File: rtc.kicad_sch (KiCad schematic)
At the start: 8 parts, among them U2901 PCF85063ATL, Y2901 32.768kHz 7pF

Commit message: Fix schematic ERC errors
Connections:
- net I2C0.SCL renamed I2C1.SCL
- net I2C0.SDA renamed I2C1.SDA

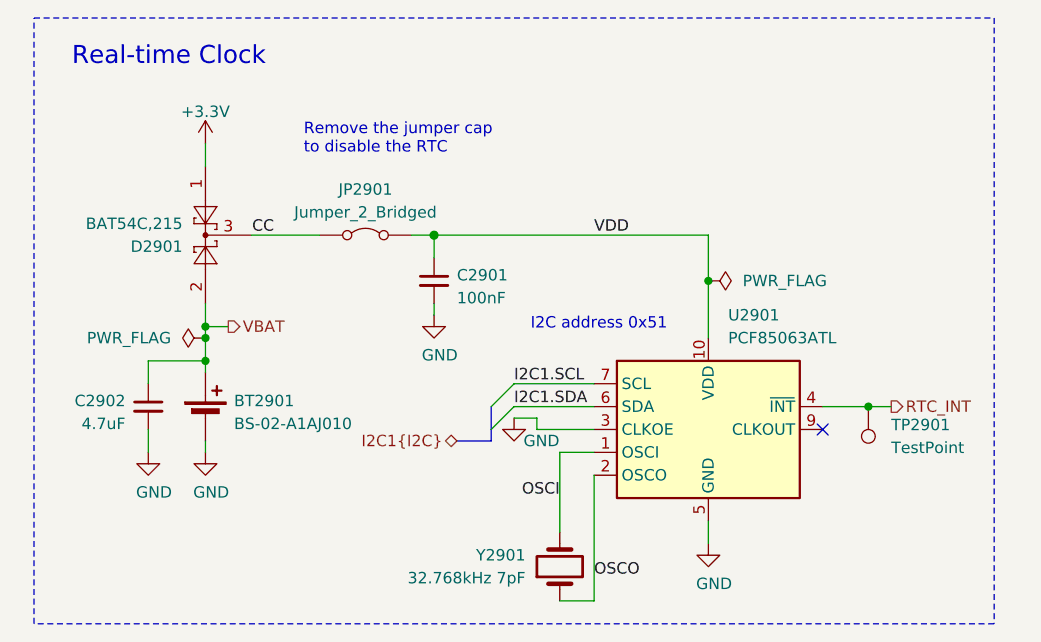
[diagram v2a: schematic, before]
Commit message: Reannotate components
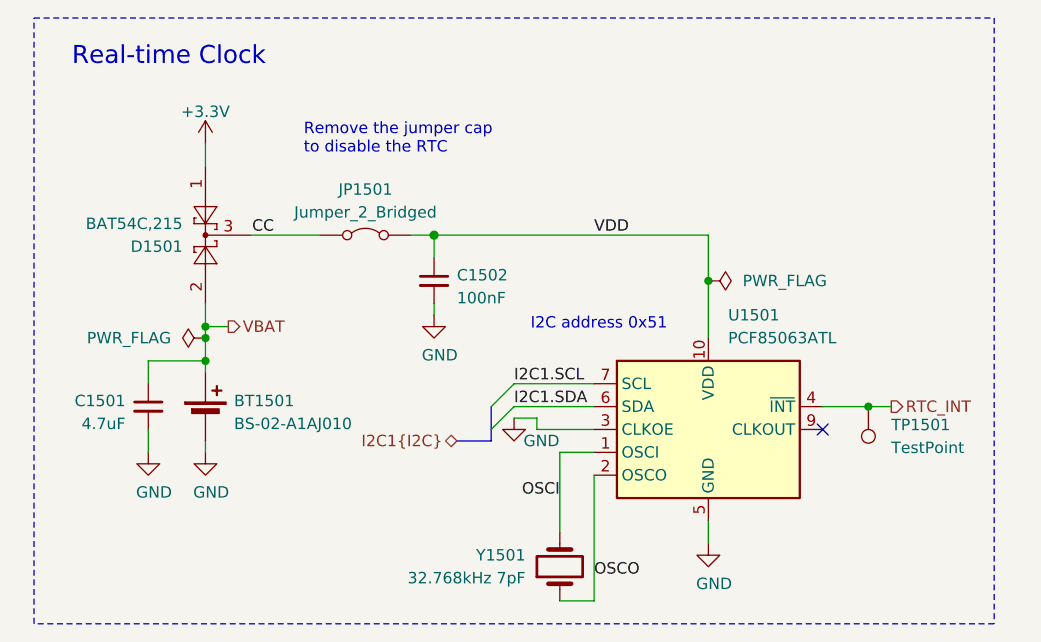
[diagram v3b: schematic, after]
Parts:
- renumbered BT2901 to BT1501, C2902 to C1501, C2901 to C1502, D2901 to D1501, JP2901 to JP1501, TP2901 to TP1501, U2901 to U1501, Y2901 to Y1501
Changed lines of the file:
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@@
 		(on_board yes)
 		(dnp no)
-		(property "Reference" "Y2901"
+		(property "Reference" "Y1501"
 			(at 147.32 118.1099 90)
 			(effects
@@
 			(project "HALPI2"
 				(path "/abc482bd-3f17-4d35-80db-1da3dcdb5c27/850df4bf-e40a-4082-adc2-76804638b949/e502b11a-b887-47b5-9ff1-f210171ce142"
-					(reference "Y2901")
+					(reference "Y1501")
 					(unit 1)
 				)
@@
 		(on_board yes)
 		(dnp no)
-		(property "Reference" "#FLG02901"
+		(property "Reference" "#FLG01502"
 			(at 169.545 87.63 0)
 			(effects
@@
 			(project "HALPI2"
 				(path "/abc482bd-3f17-4d35-80db-1da3dcdb5c27/850df4bf-e40a-4082-adc2-76804638b949/e502b11a-b887-47b5-9ff1-f210171ce142"
-					(reference "#FLG02901")
+					(reference "#FLG01502")
 					(unit 1)
 				)
@@
 		(on_board yes)
 		(dnp no)
-		(property "Reference" "D2901"
+		(property "Reference" "D1501"
 			(at 109.22 83.82 90)
 			(effects
@@
 			(project "HALPI2"
 				(path "/abc482bd-3f17-4d35-80db-1da3dcdb5c27/850df4bf-e40a-4082-adc2-76804638b949/e502b11a-b887-47b5-9ff1-f210171ce142"
-					(reference "D2901")
+					(reference "D1501")
 					(unit 1)
 				)
@@
 		(on_board yes)
 		(dnp no)
-		(property "Reference" "#PWR02907"
+		(property "Reference" "#PWR01506"
 			(at 167.64 123.19 0)
 			(effects
@@
 			(project "HALPI2"
 				(path "/abc482bd-3f17-4d35-80db-1da3dcdb5c27/850df4bf-e40a-4082-adc2-76804638b949/e502b11a-b887-47b5-9ff1-f210171ce142"
-					(reference "#PWR02907")
+					(reference "#PWR01506")
 					(unit 1)
 				)
@@
 		(on_board yes)
 		(dnp no)
-		(property "Reference" "TP2901"
+		(property "Reference" "TP1501"
 			(at 187.96 103.6319 0)
 			(effects
@@
 			(project "HALPI2"
 				(path "/abc482bd-3f17-4d35-80db-1da3dcdb5c27/850df4bf-e40a-4082-adc2-76804638b949/e502b11a-b887-47b5-9ff1-f210171ce142"
-					(reference "TP2901")
+					(reference "TP1501")
 					(unit 1)
 				)
@@
 		(on_board yes)
 		(dnp no)
-		(property "Reference" "BT2901"
+		(property "Reference" "BT1501"
 			(at 114.935 100.965 0)
 			(effects
@@
 			(project "HALPI2"
 				(path "/abc482bd-3f17-4d35-80db-1da3dcdb5c27/850df4bf-e40a-4082-adc2-76804638b949/e502b11a-b887-47b5-9ff1-f210171ce142"
-					(reference "BT2901")
+					(reference "BT1501")
 					(unit 1)
 				)
@@
 		(on_board yes)
 		(dnp no)
-		(property "Reference" "#PWR02905"
+		(property "Reference" "#PWR01503"
 			(at 111.76 113.03 0)
 			(effects
@@
 			(project "HALPI2"
 				(path "/abc482bd-3f17-4d35-80db-1da3dcdb5c27/850df4bf-e40a-4082-adc2-76804638b949/e502b11a-b887-47b5-9ff1-f210171ce142"
-					(reference "#PWR02905")
+					(reference "#PWR01503")
 					(unit 1)
 				)
@@
 		(on_board yes)
 		(dnp no)
-		(property "Reference" "#PWR02902"
+		(property "Reference" "#PWR01504"
 			(at 137.16 97.79 0)
 			(effects
@@
 			(project "HALPI2"
 				(path "/abc482bd-3f17-4d35-80db-1da3dcdb5c27/850df4bf-e40a-4082-adc2-76804638b949/e502b11a-b887-47b5-9ff1-f210171ce142"
-					(reference "#PWR02902")
+					(reference "#PWR01504")
 					(unit 1)
 				)
@@
 		(dnp no)
 		(fields_autoplaced yes)
-		(property "Reference" "U2901"
+		(property "Reference" "U1501"
 			(at 169.8341 91.44 0)
 			(effects
@@
 			(project "HALPI2"
 				(path "/abc482bd-3f17-4d35-80db-1da3dcdb5c27/850df4bf-e40a-4082-adc2-76804638b949/e502b11a-b887-47b5-9ff1-f210171ce142"
-					(reference "U2901")
+					(reference "U1501")
 					(unit 1)
 				)
@@
 		(on_board yes)
 		(dnp no)
-		(property "Reference" "#FLG02902"
+		(property "Reference" "#FLG01501"
 			(at 109.855 93.98 0)
 			(effects
@@
 			(project "HALPI2"
 				(path "/abc482bd-3f17-4d35-80db-1da3dcdb5c27/850df4bf-e40a-4082-adc2-76804638b949/e502b11a-b887-47b5-9ff1-f210171ce142"
-					(reference "#FLG02902")
+					(reference "#FLG01501")
 					(unit 1)
 				)
@@
 		(on_board yes)
 		(dnp no)
-		(property "Reference" "#PWR02904"
+		(property "Reference" "#PWR01501"
 			(at 105.41 113.03 0)
 			(effects
@@
 			(project "HALPI2"
 				(path "/abc482bd-3f17-4d35-80db-1da3dcdb5c27/850df4bf-e40a-4082-adc2-76804638b949/e502b11a-b887-47b5-9ff1-f210171ce142"
-					(reference "#PWR02904")
+					(reference "#PWR01501")
 					(unit 1)
 				)
@@
 		(on_board yes)
 		(dnp no)
-		(property "Reference" "#PWR02901"
+		(property "Reference" "#PWR01502"
 			(at 115.57 73.66 0)
 			(effects
@@
 			(project "HALPI2"
 				(path "/abc482bd-3f17-4d35-80db-1da3dcdb5c27/850df4bf-e40a-4082-adc2-76804638b949/e502b11a-b887-47b5-9ff1-f210171ce142"
-					(reference "#PWR02901")
+					(reference "#PWR01502")
 					(unit 1)
 				)
@@
 		(on_board yes)
 		(dnp no)
-		(property "Reference" "C2902"
+		(property "Reference" "C1501"
 			(at 102.87 100.965 0)
 			(effects
@@
 			(project "HALPI2"
 				(path "/abc482bd-3f17-4d35-80db-1da3dcdb5c27/850df4bf-e40a-4082-adc2-76804638b949/e502b11a-b887-47b5-9ff1-f210171ce142"
-					(reference "C2902")
+					(reference "C1501")
 					(unit 1)
 				)
@@
 		(dnp no)
 		(fields_autoplaced yes)
-		(property "Reference" "JP2901"
+		(property "Reference" "JP1501"
 			(at 129.54 77.47 0)
 			(effects
@@
 			(project "HALPI2"
 				(path "/abc482bd-3f17-4d35-80db-1da3dcdb5c27/850df4bf-e40a-4082-adc2-76804638b949/e502b11a-b887-47b5-9ff1-f210171ce142"
-					(reference "JP2901")
+					(reference "JP1501")
 					(unit 1)
 				)
@@
 		(on_board yes)
 		(dnp no)
-		(property "Reference" "C2901"
+		(property "Reference" "C1502"
 			(at 139.7 86.995 0)
 			(effects
@@
 			(project "HALPI2"
 				(path "/abc482bd-3f17-4d35-80db-1da3dcdb5c27/850df4bf-e40a-4082-adc2-76804638b949/e502b11a-b887-47b5-9ff1-f210171ce142"
-					(reference "C2901")
+					(reference "C1502")
 					(unit 1)
 				)
@@
 		(on_board yes)
 		(dnp no)
-		(property "Reference" "#PWR02903"
+		(property "Reference" "#PWR01505"
 			(at 146.05 109.22 0)
 			(effects
@@
 			(project "HALPI2"
 				(path "/abc482bd-3f17-4d35-80db-1da3dcdb5c27/850df4bf-e40a-4082-adc2-76804638b949/e502b11a-b887-47b5-9ff1-f210171ce142"
-					(reference "#PWR02903")
-					(unit 1)
-				)
+					(reference "#PWR01505")
+					(unit 1)
+				)

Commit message: Silkscreen mostly done
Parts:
- removed C1501: 4.7uF, Capacitor_SMD:C_0402_1005Metric, symbol Device:C_Small
- C1502: value 100nF -> 1uF; LCSC C1525 -> C52923
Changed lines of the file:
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@@
-	)
-	(junction
-		(at 111.76 96.52)
-		(diameter 0)
-		(color 0 0 0 0)
 	)
 	(junction
@@
 	(wire
 		(pts
-			(xy 105.41 96.52) (xy 111.76 96.52)
-		)
-		(stroke
-			(width 0)
-			(type default)
-		)
-	)
-	(wire
-		(pts
-			(xy 111.76 93.98) (xy 111.76 96.52)
-		)
-		(stroke
-			(width 0)
-			(type solid)
-		)
-	)
-	(wire
-		(pts
 			(xy 137.16 82.55) (xy 137.16 85.09)
 		)
@@
 	(wire
 		(pts
-			(xy 105.41 99.06) (xy 105.41 96.52)
-		)
-		(stroke
-			(width 0)
-			(type default)
-		)
-	)
-	(wire
-		(pts
-			(xy 105.41 104.14) (xy 105.41 106.68)
-		)
-		(stroke
-			(width 0)
-			(type default)
-		)
-	)
-	(wire
-		(pts
-			(xy 111.76 96.52) (xy 111.76 97.79)
+			(xy 111.76 93.98) (xy 111.76 97.79)
 		)
 		(stroke
@@
 		(length 2.54)
 		(shape round)
-		(at 105.41 97.79 90)
+		(at 111.76 97.79 270)
 		(fields_autoplaced yes)
 		(effects
@@
 				(size 1.27 1.27)
 			)
-			(justify left bottom)
+			(justify right bottom)
 		)
 		(property "Netclass" "Power"
-			(at 102.87 96.901 90)
+			(at 114.3 96.901 90)
 			(effects
 				(font
@@
 		(lib_id "Device:Battery_Cell")
 		(at 111.76 102.87 0)
+		(mirror y)
 		(unit 1)
 		(exclude_from_sim no)
@@
 		(dnp no)
 		(property "Reference" "BT1501"
-			(at 114.935 100.965 0)
+			(at 108.585 100.965 0)
 			(effects
 				(font
@@
 		)
 		(property "Value" "BS-02-A1AJ010"
-			(at 114.935 103.505 0)
+			(at 108.585 103.505 0)
 			(effects
 				(font
@@
 	)
 	(symbol
-		(lib_id "power:GND")
-		(at 105.41 106.68 0)
-		(unit 1)
-		(exclude_from_sim no)
-		(in_bom yes)
-		(on_board yes)
-		(dnp no)
-		(property "Reference" "#PWR01501"
-			(at 105.41 113.03 0)
-			(effects
-				(font
-					(size 1.27 1.27)
-				)
-				(hide yes)
-			)
-		)
-		(property "Value" "GND"
-			(at 106.045 111.125 0)
-			(effects
-				(font
-					(size 1.27 1.27)
-				)
-			)
-		)
-		(property "Footprint" ""
-			(at 105.41 106.68 0)
-			(effects
-				(font
-					(size 1.27 1.27)
-				)
-				(hide yes)
-			)
-		)
-		(property "Datasheet" ""
-			(at 105.41 106.68 0)
-			(effects
-				(font
-					(size 1.27 1.27)
-				)
-				(hide yes)
-			)
-		)
-		(property "Description" "Power symbol creates a global label with name \"GND\" , ground"
-			(at 105.41 106.68 0)
-			(effects
-				(font
-					(size 1.27 1.27)
-				)
-				(hide yes)
-			)
-		)
-		(pin "1"
-		)
-		(instances
-			(project "HALPI2"
-				(path "/abc482bd-3f17-4d35-80db-1da3dcdb5c27/850df4bf-e40a-4082-adc2-76804638b949/e502b11a-b887-47b5-9ff1-f210171ce142"
-					(reference "#PWR01501")
-					(unit 1)
-				)
-			)
-		)
-	)
-	(symbol
 		(lib_id "power:+3.3V")
 		(at 111.76 72.39 0)
@@
 				(path "/abc482bd-3f17-4d35-80db-1da3dcdb5c27/850df4bf-e40a-4082-adc2-76804638b949/e502b11a-b887-47b5-9ff1-f210171ce142"
 					(reference "#PWR01502")
-					(unit 1)
-				)
-			)
-		)
-	)
-	(symbol
-		(lib_id "Device:C_Small")
-		(at 105.41 101.6 0)
-		(mirror y)
-		(unit 1)
-		(exclude_from_sim no)
-		(in_bom yes)
-		(on_board yes)
-		(dnp no)
-		(property "Reference" "C1501"
-			(at 102.87 100.965 0)
-			(effects
-				(font
-					(size 1.27 1.27)
-				)
-				(justify left)
-			)
-		)
-		(property "Value" "4.7uF"
-			(at 102.87 103.505 0)
-			(effects
-				(font
-					(size 1.27 1.27)
-				)
-				(justify left)
-			)
-		)
-		(property "Footprint" "Capacitor_SMD:C_0402_1005Metric"
-			(at 105.41 101.6 0)
-			(effects
-				(font
-					(size 1.27 1.27)
-				)
-				(hide yes)
-			)
-		)
-		(property "Datasheet" "~"
-			(at 105.41 101.6 0)
-			(effects
-				(font
-					(size 1.27 1.27)
-				)
-				(hide yes)
-			)
-		)
-		(property "Description" ""
-			(at 105.41 101.6 0)
-			(effects
-				(font
-					(size 1.27 1.27)
-				)
-				(hide yes)
-			)
-		)
-		(property "LCSC" "C23733"
-			(at 105.41 101.6 0)
-			(effects
-				(font
-					(size 1.27 1.27)
-				)
-				(hide yes)
-			)
-		)
-		(property "Characteristics" ""
-			(at 105.41 101.6 0)
-			(effects
-				(font
-					(size 1.27 1.27)
-				)
-				(hide yes)
-			)
-		)
-		(pin "1"
-		)
-		(pin "2"
-		)
-		(instances
-			(project "HALPI2"
-				(path "/abc482bd-3f17-4d35-80db-1da3dcdb5c27/850df4bf-e40a-4082-adc2-76804638b949/e502b11a-b887-47b5-9ff1-f210171ce142"
-					(reference "C1501")
 					(unit 1)
 				)
@@
 			)
 		)
-		(property "Value" "100nF"
+		(property "Value" "1uF"
 			(at 139.7 89.535 0)
 			(effects
@@
 			)
 		)
-		(property "LCSC" "C1525"
+		(property "LCSC" "C52923"
 			(at 137.16 87.63 0)
 			(effects

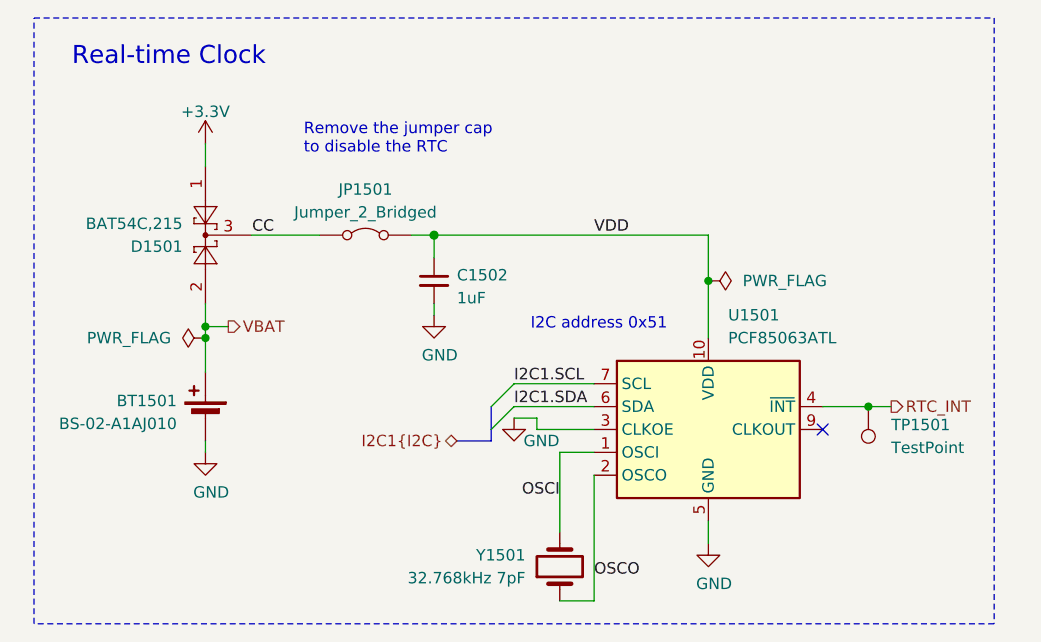
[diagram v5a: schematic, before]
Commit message: Finish the board redesign with SoM on the bottom
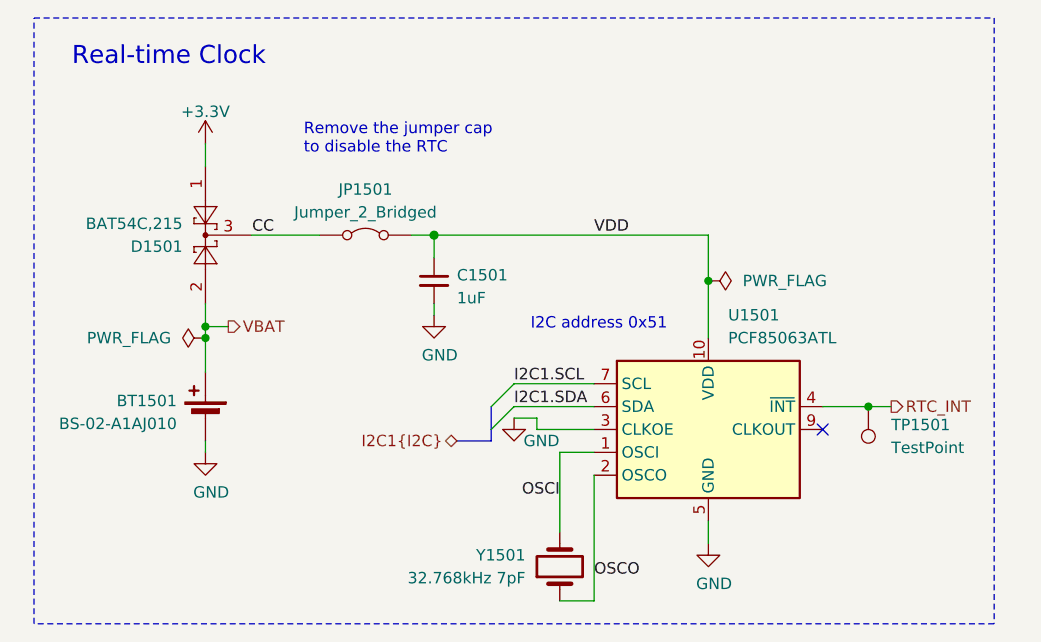
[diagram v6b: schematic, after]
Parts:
- renumbered C1502 to C1501
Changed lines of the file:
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@@
 			)
 		)
-		(property "Description" ""
+		(property "Description" "Two pin crystal"
 			(at 151.13 119.38 0)
 			(effects
@@
 			)
 		)
-		(property "Description" ""
+		(property "Description" "dual schottky barrier diode, common cathode"
 			(at 111.76 82.55 0)
 			(effects
@@
 		(on_board yes)
 		(dnp no)
-		(property "Reference" "#PWR01506"
+		(property "Reference" "#PWR01505"
 			(at 167.64 123.19 0)
 			(effects
@@
 			(project "HALPI2"
 				(path "/abc482bd-3f17-4d35-80db-1da3dcdb5c27/850df4bf-e40a-4082-adc2-76804638b949/e502b11a-b887-47b5-9ff1-f210171ce142"
-					(reference "#PWR01506")
+					(reference "#PWR01505")
 					(unit 1)
 				)
@@
 		(on_board yes)
 		(dnp no)
-		(property "Reference" "#PWR01503"
+		(property "Reference" "#PWR01502"
 			(at 111.76 113.03 0)
 			(effects
@@
 			(project "HALPI2"
 				(path "/abc482bd-3f17-4d35-80db-1da3dcdb5c27/850df4bf-e40a-4082-adc2-76804638b949/e502b11a-b887-47b5-9ff1-f210171ce142"
-					(reference "#PWR01503")
+					(reference "#PWR01502")
 					(unit 1)
 				)
@@
 		(on_board yes)
 		(dnp no)
-		(property "Reference" "#PWR01504"
+		(property "Reference" "#PWR01503"
 			(at 137.16 97.79 0)
 			(effects
@@
 			(project "HALPI2"
 				(path "/abc482bd-3f17-4d35-80db-1da3dcdb5c27/850df4bf-e40a-4082-adc2-76804638b949/e502b11a-b887-47b5-9ff1-f210171ce142"
-					(reference "#PWR01504")
+					(reference "#PWR01503")
 					(unit 1)
 				)
@@
 		(on_board yes)
 		(dnp no)
-		(property "Reference" "#PWR01502"
+		(property "Reference" "#PWR01501"
 			(at 115.57 73.66 0)
 			(effects
@@
 			(project "HALPI2"
 				(path "/abc482bd-3f17-4d35-80db-1da3dcdb5c27/850df4bf-e40a-4082-adc2-76804638b949/e502b11a-b887-47b5-9ff1-f210171ce142"
-					(reference "#PWR01502")
+					(reference "#PWR01501")
 					(unit 1)
 				)
@@
 		(on_board yes)
 		(dnp no)
-		(property "Reference" "C1502"
+		(property "Reference" "C1501"
 			(at 139.7 86.995 0)
 			(effects
@@
 			)
 		)
-		(property "Description" ""
+		(property "Description" "Unpolarized capacitor, small symbol"
 			(at 137.16 87.63 0)
 			(effects
@@
 			(project "HALPI2"
 				(path "/abc482bd-3f17-4d35-80db-1da3dcdb5c27/850df4bf-e40a-4082-adc2-76804638b949/e502b11a-b887-47b5-9ff1-f210171ce142"
-					(reference "C1502")
+					(reference "C1501")
 					(unit 1)
 				)
@@
 		(on_board yes)
 		(dnp no)
-		(property "Reference" "#PWR01505"
+		(property "Reference" "#PWR01504"
 			(at 146.05 109.22 0)
 			(effects
@@
 			(project "HALPI2"
 				(path "/abc482bd-3f17-4d35-80db-1da3dcdb5c27/850df4bf-e40a-4082-adc2-76804638b949/e502b11a-b887-47b5-9ff1-f210171ce142"
-					(reference "#PWR01505")
-					(unit 1)
-				)
+					(reference "#PWR01504")
+					(unit 1)
+				)

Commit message: Further refinements
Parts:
- added TP1206: TestPoint, TestPoint:TestPoint_Pad_D1.0mm, symbol Connector:TestPoint
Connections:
- net VBAT: now also TP1206.1
- net RTC_INT renamed ~{RTC_INT}
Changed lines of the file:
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@@
+	)
+	(junction
+		(at 111.76 90.17)
+		(diameter 0)
+		(color 0 0 0 0)
 	)
 	(junction
@@
 			(width 0)
 			(type solid)
+		)
+	)
+	(wire
+		(pts
+			(xy 101.6 90.17) (xy 111.76 90.17)
+		)
+		(stroke
+			(width 0)
+			(type default)
 		)
 	)
@@
 		)
 	)
-	(hierarchical_label "RTC_INT"
+	(hierarchical_label "~{RTC_INT}"
 		(shape output)
 		(at 187.96 101.6 0)
@@
 				)
 				(hide yes)
+			)
+		)
+		(property "LCSC Part" ""
+			(at 151.13 119.38 0)
+			(effects
+				(font
+					(size 1.27 1.27)
+				)
+			)
+		)
+		(property "Sim.Enable" ""
+			(at 151.13 119.38 0)
+			(effects
+				(font
+					(size 1.27 1.27)
+				)
 			)
 		)
@@
 			)
 		)
+		(property "LCSC Part" ""
+			(at 111.76 82.55 0)
+			(effects
+				(font
+					(size 1.27 1.27)
+				)
+			)
+		)
+		(property "Sim.Enable" ""
+			(at 111.76 82.55 0)
+			(effects
+				(font
+					(size 1.27 1.27)
+				)
+			)
+		)
 		(pin "1"
 		)
@@
 				)
 				(hide yes)
+			)
+		)
+		(property "LCSC Part" ""
+			(at 185.42 101.6 0)
+			(effects
+				(font
+					(size 1.27 1.27)
+				)
+			)
+		)
+		(property "Sim.Enable" ""
+			(at 185.42 101.6 0)
+			(effects
+				(font
+					(size 1.27 1.27)
+				)
 			)
 		)
@@
 			)
 		)
+		(property "LCSC Part" ""
+			(at 111.76 102.87 0)
+			(effects
+				(font
+					(size 1.27 1.27)
+				)
+			)
+		)
+		(property "Sim.Enable" ""
+			(at 111.76 102.87 0)
+			(effects
+				(font
+					(size 1.27 1.27)
+				)
+			)
+		)
 		(pin "1"
 		)
@@
 			)
 		)
+		(property "LCSC Part" ""
+			(at 167.64 104.14 0)
+			(effects
+				(font
+					(size 1.27 1.27)
+				)
+			)
+		)
+		(property "Sim.Enable" ""
+			(at 167.64 104.14 0)
+			(effects
+				(font
+					(size 1.27 1.27)
+				)
+			)
+		)
 		(pin "6"
 		)
@@
 			)
 		)
+		(property "LCSC Part" ""
+			(at 129.54 82.55 0)
+			(effects
+				(font
+					(size 1.27 1.27)
+				)
+			)
+		)
+		(property "Sim.Enable" ""
+			(at 129.54 82.55 0)
+			(effects
+				(font
+					(size 1.27 1.27)
+				)
+			)
+		)
 		(pin "2"
 		)
@@
 			)
 		)
+		(property "LCSC Part" ""
+			(at 137.16 87.63 0)
+			(effects
+				(font
+					(size 1.27 1.27)
+				)
+			)
+		)
+		(property "Sim.Enable" ""
+			(at 137.16 87.63 0)
+			(effects
+				(font
+					(size 1.27 1.27)
+				)
+			)
+		)
 		(pin "1"
 		)
@@
 					(unit 1)
 				)
+			)
+		)
+	)
+	(symbol
+		(lib_id "Connector:TestPoint")
+		(at 101.6 90.17 90)
+		(mirror x)
+		(unit 1)
+		(exclude_from_sim no)
+		(in_bom yes)
+		(on_board yes)
+		(dnp no)
+		(fields_autoplaced yes)
+		(property "Reference" "TP1206"
+			(at 98.298 85.09 90)
+			(effects
+				(font
+					(size 1.27 1.27)
+				)
+			)
+		)
+		(property "Value" "TestPoint"
+			(at 98.298 87.63 90)
+			(effects
+				(font
+					(size 1.27 1.27)
+				)
+			)
+		)
+		(property "Footprint" "TestPoint:TestPoint_Pad_D1.0mm"
+			(at 101.6 95.25 0)
+			(effects
+				(font
+					(size 1.27 1.27)
+				)
+				(hide yes)
+			)
+		)
+		(property "Datasheet" "~"
+			(at 101.6 95.25 0)
+			(effects
+				(font
+					(size 1.27 1.27)
+				)
+				(hide yes)
+			)
+		)
+		(property "Description" "test point"
+			(at 101.6 90.17 0)
+			(effects
+				(font
+					(size 1.27 1.27)
+				)
+				(hide yes)
+			)
+		)
+		(property "Characteristics" ""
+			(at 101.6 90.17 0)
+			(effects
+				(font
+					(size 1.27 1.27)
+				)
+				(hide yes)
+			)
+		)
+		(property "LCSC Part" ""
+			(at 101.6 90.17 0)
+			(effects
+				(font
+					(size 1.27 1.27)
+				)
+			)
+		)
+		(property "Sim.Enable" ""
+			(at 101.6 90.17 0)
+			(effects
+				(font
+					(size 1.27 1.27)
+				)
+			)
+		)
+		(pin "1"
+		)
+		(instances
+			(project "HALPI2"
+				(path "/abc482bd-3f17-4d35-80db-1da3dcdb5c27/850df4bf-e40a-4082-adc2-76804638b949/e502b11a-b887-47b5-9ff1-f210171ce142"
+					(reference "TP1206")
+					(unit 1)
+				)
